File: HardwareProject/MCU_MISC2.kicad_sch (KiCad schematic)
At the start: 25 parts, among them J1 USB_B, J2 USB_C_Receptacle_USB2.0_16P, J3 Conn_02x16_Odd_Even, Q5 S8050, Q7 S8050, U5 TPD4E05U06DQA

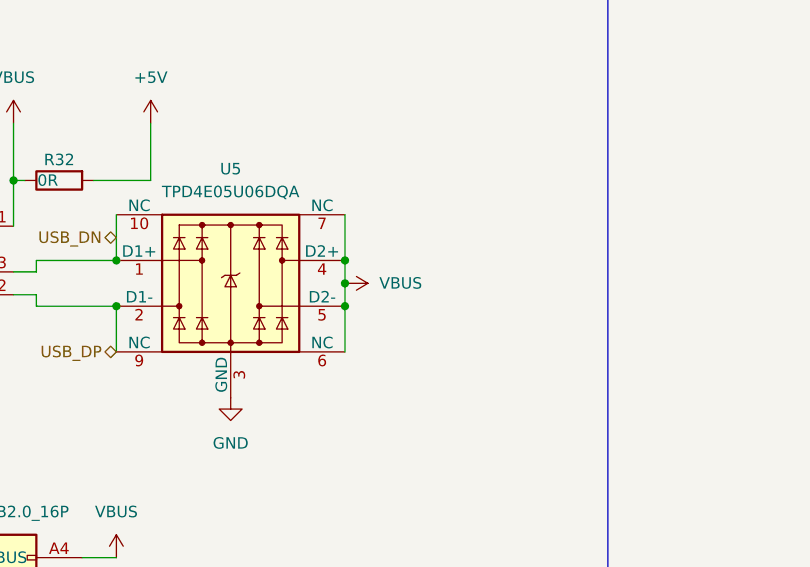
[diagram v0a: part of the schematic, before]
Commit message: 修改了UCC27211A封装，此芯片此前的封装均错误 修改了采样线布局，为SAR ADC加入前置RC
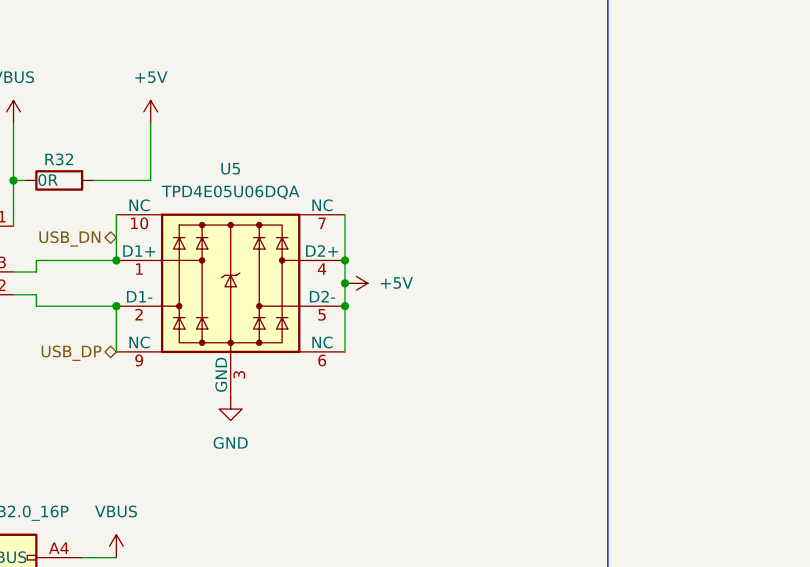
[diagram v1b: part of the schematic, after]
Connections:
- net +5V: now also U5.4 (D2+), U5.5 (D2-), U5.6 (NC), U5.7 (NC)
- net VBUS: no longer U5.4 (D2+), U5.5 (D2-), U5.6 (NC), U5.7 (NC)
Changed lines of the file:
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@@
 	)
 	(junction
+		(at 85.09 44.45)
+		(diameter 0)
+		(color 0 0 0 0)
+	)
+	(junction
 		(at 212.09 128.27)
 		(diameter 0)
@@
 	)
 	(junction
-		(at 85.09 44.45)
-		(diameter 0)
-		(color 0 0 0 0)
-	)
-	(junction
 		(at 201.93 41.91)
 		(diameter 0)
@@
 	(wire
 		(pts
+			(xy 85.09 44.45) (xy 85.09 46.99)
+		)
+		(stroke
+			(width 0)
+			(type default)
+		)
+	)
+	(wire
+		(pts
 			(xy 231.14 140.97) (xy 247.65 140.97)
 		)
@@
 	(wire
 		(pts
-			(xy 85.09 44.45) (xy 85.09 46.99)
+			(xy 85.09 41.91) (xy 85.09 44.45)
 		)
 		(stroke
@@
 	(wire
 		(pts
-			(xy 85.09 41.91) (xy 85.09 44.45)
-		)
-		(stroke
-			(width 0)
-			(type default)
-		)
-	)
-	(wire
-		(pts
 			(xy 50.8 157.48) (xy 50.8 151.13)
 		)
@@
 	)
 	(symbol
+		(lib_id "power:+5V")
+		(at 85.09 44.45 270)
+		(unit 1)
+		(exclude_from_sim no)
+		(in_bom yes)
+		(on_board yes)
+		(dnp no)
+		(fields_autoplaced yes)
+		(property "Reference" "#PWR075"
+			(at 81.28 44.45 0)
+			(effects
+				(font
+					(size 1.27 1.27)
+				)
+				(hide yes)
+			)
+		)
+		(property "Value" "+5V"
+			(at 88.9 44.4499 90)
+			(effects
+				(font
+					(size 1.27 1.27)
+				)
+				(justify left)
+			)
+		)
+		(property "Footprint" ""
+			(at 85.09 44.45 0)
+			(effects
+				(font
+					(size 1.27 1.27)
+				)
+				(hide yes)
+			)
+		)
+		(property "Datasheet" ""
+			(at 85.09 44.45 0)
+			(effects
+				(font
+					(size 1.27 1.27)
+				)
+				(hide yes)
+			)
+		)
+		(property "Description" ""
+			(at 85.09 44.45 0)
+			(effects
+				(font
+					(size 1.27 1.27)
+				)
+				(hide yes)
+			)
+		)
+		(pin "1"
+		)
+		(instances
+			(project "HPM6P41_BB"
+				(path "/714b8a30-f9a7-49d4-a000-bc20c4884c7a/8753c7ec-cb46-4092-8be3-4a324384953b"
+					(reference "#PWR075")
+					(unit 1)
+				)
+			)
+		)
+	)
+	(symbol
 		(lib_id "Device:R")
 		(at 46.99 157.48 90)
@@
 					(unit 1)
 				)
-			)
-		)
-	)
-	(symbol
-		(lib_id "power:VBUS")
-		(at 85.09 44.45 270)
-		(unit 1)
-		(exclude_from_sim no)
-		(in_bom yes)
-		(on_board yes)
-		(dnp no)
-		(fields_autoplaced yes)
-		(property "Reference" "#PWR075"
-			(at 81.28 44.45 0)
-			(effects
-				(font
-					(size 1.27 1.27)
-				)
-				(hide yes)
-			)
-		)
-		(property "Value" "VBUS"
-			(at 88.9 44.4499 90)
-			(effects
-				(font
-					(size 1.27 1.27)
-				)
-				(justify left)
-			)
-		)
-		(property "Footprint" ""
-			(at 85.09 44.45 0)
-			(effects
-				(font
-					(size 1.27 1.27)
-				)
-				(hide yes)
-			)
-		)
-		(property "Datasheet" ""
-			(at 85.09 44.45 0)
-			(effects
-				(font
-					(size 1.27 1.27)
-				)
-				(hide yes)
-			)
-		)
-		(property "Description" "Power symbol creates a global label with name \"VBUS\""
-			(at 85.09 44.45 0)
-			(effects
-				(font
-					(size 1.27 1.27)
-				)
-				(hide yes)
-			)
-		)
-		(pin "1"
-		)
-		(instances
-			(project "HPM6P41_BB"
-				(path "/714b8a30-f9a7-49d4-a000-bc20c4884c7a/8753c7ec-cb46-4092-8be3-4a324384953b"
-					(reference "#PWR075")
-					(unit 1)
-				)

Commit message: 外置核心电压SYR838以改善ADC噪声
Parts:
- R32, R70: value 0R -> 0Ω
- R72: value 100 -> 100Ω
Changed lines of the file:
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@@
 			)
 		)
-		(property "Value" "100"
+		(property "Value" "100Ω"
 			(at 57.15 151.13 90)
 			(effects
@@
 			)
 		)
-		(property "Value" "0R"
-			(at 43.18 135.89 90)
+		(property "Value" "0Ω"
+			(at 43.18 137.16 90)
 			(effects
 				(font
@@
 			)
 		)
-		(property "Value" "0R"
-			(at 52.07 33.02 90)
-			(effects
-				(font
+		(property "Value" "0Ω"
+			(at 53.34 33.02 90)
+			(effects
+				(font

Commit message: 换其他电感之前暂存一下
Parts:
- removed J1: USB_B, HPM6P41_BB:USB_B_OST_USB-B1HSxx_Horizontal, symbol Connector:USB_B
- removed J3: Conn_02x16_Odd_Even, Connector_PinHeader_2.54mm:PinHeader_2x16_P2.54mm_Vertical, symbol Connector_Generic:Conn_02x16_Odd_Even
- removed R32: 0Ω, Resistor_SMD:R_0805_2012Metric, symbol Device:R
- added C36, C39: 100nF, Capacitor_SMD:C_0603_1608Metric, symbol Device:C
- added C40, C41: 1uF,10V, Capacitor_SMD:C_0603_1608Metric, symbol Device:C
- added J1, J13, J14: 排针, Connector_PinHeader_2.54mm:PinHeader_1x02_P2.54mm_Vertical, symbol Connector:Conn_01x02_Pin
- added J4: Conn_ARM_JTAG_SWD_20, Connector_IDC:IDC-Header_2x10_P2.54mm_Vertical, symbol Connector:Conn_ARM_JTAG_SWD_20
- added U24: CA-IS3762HN, kicad_community_lib:CA-IS3762HN, symbol CA-IS3762HN:CA-IS3762HN
- added U26: XC6206PxxxMR, Package_TO_SOT_SMD:SOT-23-3, symbol Regulator_Linear:XC6206PxxxMR
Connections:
- net +3.3V: now also C39.2, U24.16 (VDDB)
- net +5V: now also J1.1 (Pin_1)
- net GND: now also C39.1, U24.9 (GNDB)
- net VBUS: now also J1.2 (Pin_2)
- new net 5V_SUPPLY: C40.1, J13.1 (Pin_1), J4.19 (DBGACK/NC), U26.3 (VI)
- new net CON_RX: J14.1 (Pin_1), U24.5 (VI4)
- new net CON_TCK: J4.9 (TCK/SWDCLK), U24.2 (VI1)
- new net CON_TDI: J4.5 (TDI), U24.4 (VI3)
- new net CON_TDO: J4.13 (TDO/SWO), U24.6 (VO5)
- new net CON_TMS: J4.7 (TMS/SWDIO), U24.3 (VI2)
- new net CON_TX: J14.2 (Pin_2), U24.7 (VO6)
- new net ISO_GND: C36.1, C40.2, C41.2, J13.2 (Pin_2), J4.10 (GND), J4.12 (GND), J4.14 (GND), J4.16 (GND), J4.18 (GND), J4.20 (GND), J4.4 (GND), J4.6 (GND), J4.8 (GND), U24.8 (GNDA), U26.1 (GND)
- new net ISO_RX: U24.12 (VO4)
- new net ISO_TX: U24.10 (VI6)
- new net TCK: U24.15 (VO1)
- new net TDI: U24.13 (VO3)
- new net TDO: U24.11 (VI5)
- new net TMS: U24.14 (VO2)
- new net VTREF: C36.2, C41.1, J4.1 (VTREF), U24.1 (VDDA), U26.2 (VO)
- no-connect marks 5 -> 10
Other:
- moved on the sheet: BZ1, C92, J2, Q7, R3, R30, R70, R71, R72, U5

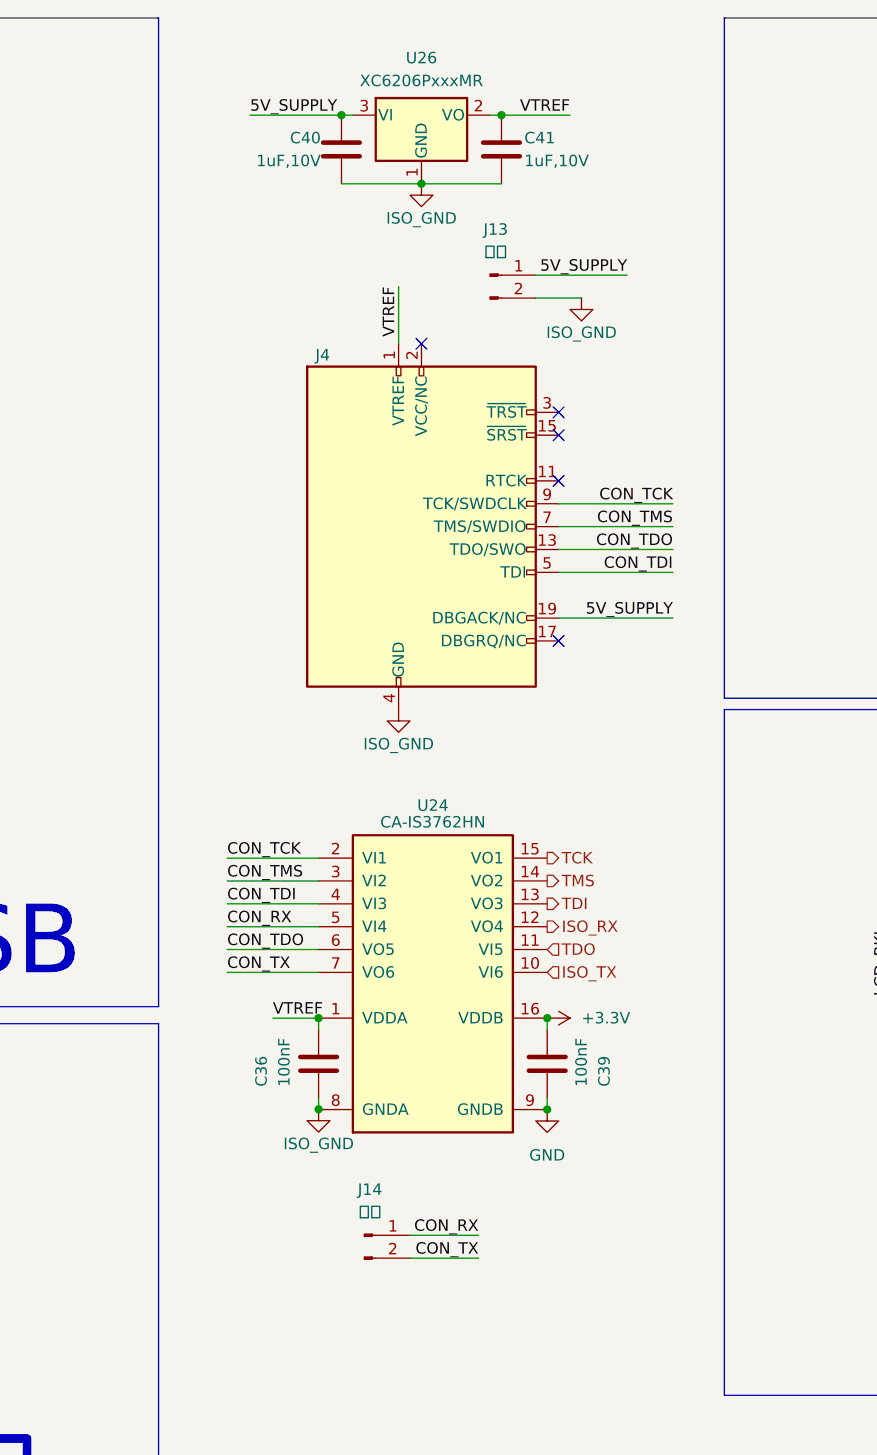
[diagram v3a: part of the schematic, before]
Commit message: 完成Rev4 电源 驱动 模拟 IO
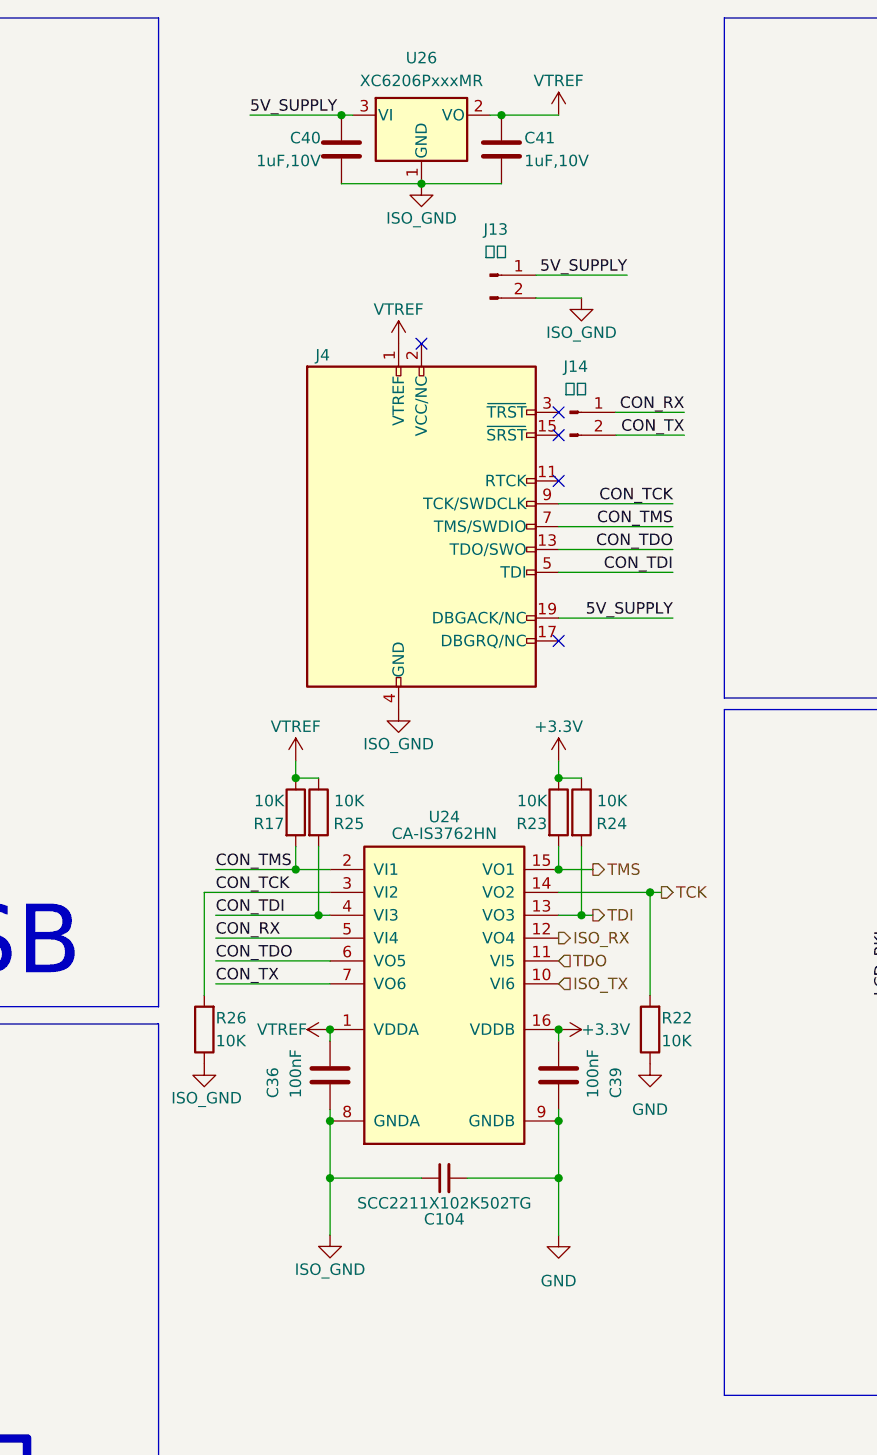
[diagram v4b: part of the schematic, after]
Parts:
- added C104: SCC2211X102K502TG, kicad_community_lib:SCC2211X102K502T, symbol SCC2211X102K502T:SCC2211X102K502T
- added R17, R22, R23, R24, R25, R26: 10K, Resistor_SMD:R_0603_1608Metric, symbol 02_HPM_Resistor:10K_0402
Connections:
- net +3.3V: now also R23.1, R24.1
- net CON_TCK: now also U24.3 (VI2), R26.2; no longer U24.2 (VI1)
- net CON_TDI: now also R25.2
- net CON_TMS: now also U24.2 (VI1), R17.2; no longer U24.3 (VI2)
- net GND: now also C104.2, R22.1
- net ISO_GND: now also C104.1, R26.1
- net TCK: now also U24.14 (VO2), R22.2; no longer U24.15 (VO1)
- net TDI: now also R24.2
- net TMS: now also U24.15 (VO1), R23.2; no longer U24.14 (VO2)
- net VTREF: now also R17.1, R25.1
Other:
- moved on the sheet: C36, C39, J14, U24

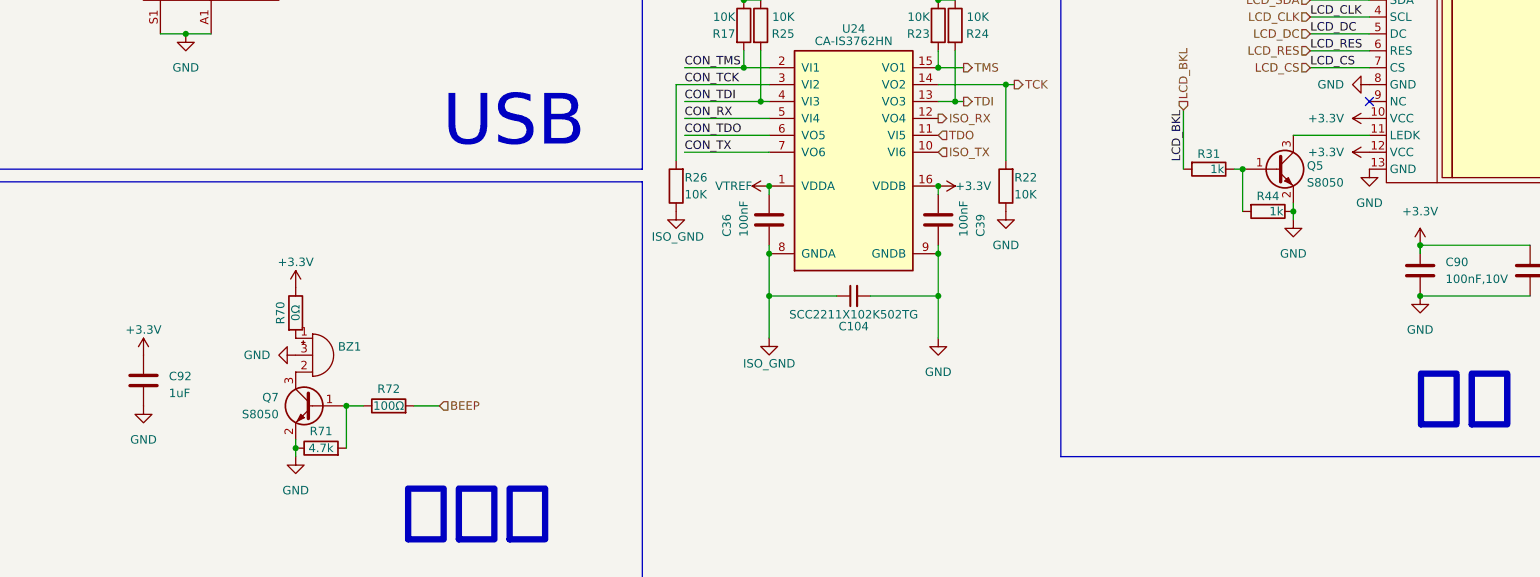
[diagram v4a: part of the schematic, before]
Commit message: 更新readme暂停通知，添加测试用例源代码
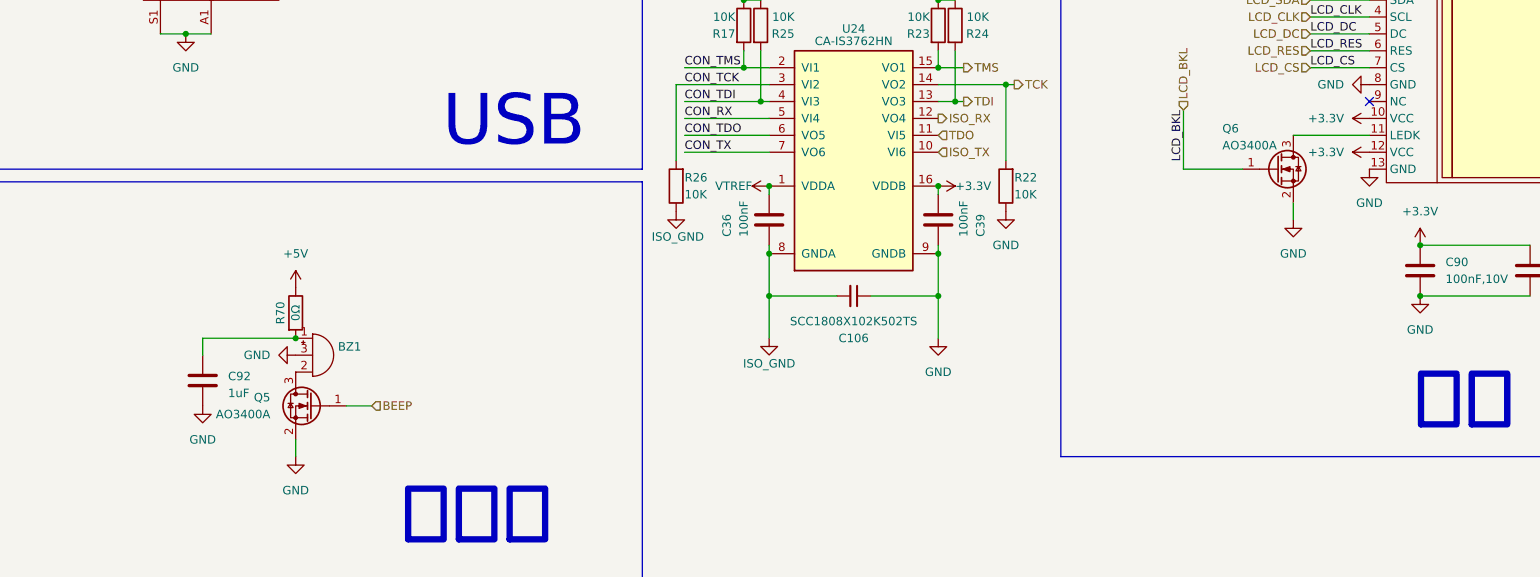
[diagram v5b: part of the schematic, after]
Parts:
- removed C104: SCC2211X102K502TG, kicad_community_lib:SCC2211X102K502T, symbol SCC2211X102K502T:SCC2211X102K502T
- removed Q5, Q7: S8050, Package_TO_SOT_SMD:SOT-23, symbol 1MyRandom:S8050
- removed R31, R44: 1k, Resistor_SMD:R_0603_1608Metric, symbol Device:R
- removed R71: 4.7k, Resistor_SMD:R_0603_1608Metric, symbol Device:R
- removed R72: 100Ω, Resistor_SMD:R_0603_1608Metric, symbol Device:R
- added C106: SCC1808X102K502TS, Capacitor_SMD:C_1808_4520Metric, symbol SCC1808X102K502TS:SCC1808X102K502TS
- added Q5, Q6: AO3400A, Package_TO_SOT_SMD:SOT-23, symbol Transistor_FET:AO3400A
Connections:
- net +3.3V: no longer C92.1, R70.1
- net +5V: now also R70.1
- net BEEP: now also Q5.1 (G)
- net GND: now also C106.1, Q5.2 (S), Q6.2 (S)
- net ISO_GND: now also C106.2
- net LCD_BKL: now also Q6.1 (G)
- net at S1.11 (LEDK): now also Q6.3 (D)
- net at BZ1.1 (+), R70.2: now also C92.1
- net at BZ1.2 (-): now also Q5.3 (D)
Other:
- moved on the sheet: C92

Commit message: rev4修改核心供电前保存（当前SYR838）
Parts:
- C76: renamed from C36; value 100nF -> 100nF,50V
- C80: renamed from C39; value 100nF -> 100nF,50V
- C81: renamed from C90; value 100nF,10V -> 100nF,50V
- C82: renamed from C91; value 100nF,10V -> 100nF,50V
- renumbered C92 to C75, C40 to C77, C106 to C78, C41 to C79, D11 to D18, D12 to D19, D15 to D20, J1 to J10, J4 to J11, J13 to J12, J14 to J13, J2 to J9, R70 to R66, R3 to R67, R30 to R68, R26 to R69, R17 to R70, R25 to R71, R23 to R72, R24 to R73, R22 to R74, R61 to R75, R62 to R76, R69 to R77, U5 to U23, U26 to U24, U24 to U25
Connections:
- net +5V: no longer U23.4 (D2+), U23.5 (D2-), U23.6 (NC), U23.7 (NC)
- net VBUS: now also U23.4 (D2+), U23.5 (D2-), U23.6 (NC), U23.7 (NC)

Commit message: Rev4保存
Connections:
- net VBUS: no longer U23.4 (D2+), U23.5 (D2-), U23.6 (NC), U23.7 (NC)
- new net: U23.4 (D2+), U23.5 (D2-), U23.6 (NC), U23.7 (NC)
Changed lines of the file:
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@@
 	)
 	(junction
-		(at 77.47 29.21)
-		(diameter 0)
-		(color 0 0 0 0)
-	)
-	(junction
 		(at 158.75 140.97)
 		(diameter 0)
@@
 	(wire
 		(pts
-			(xy 77.47 26.67) (xy 77.47 29.21)
+			(xy 77.47 26.67) (xy 77.47 31.75)
 		)
 		(stroke
@@
 	(wire
 		(pts
-			(xy 88.9 29.21) (xy 77.47 29.21)
-		)
-		(stroke
-			(width 0)
-			(type default)
-		)
-	)
-	(wire
-		(pts
 			(xy 143.51 30.48) (xy 152.4 30.48)
 		)
@@
 	(wire
 		(pts
-			(xy 77.47 29.21) (xy 77.47 31.75)
-		)
-		(stroke
-			(width 0)
-			(type default)
-		)
-	)
-	(wire
-		(pts
 			(xy 77.47 63.5) (xy 86.36 63.5)
 		)
@@
 					(unit 1)
 				)
-			)
-		)
-	)
-	(symbol
-		(lib_id "power:VBUS")
-		(at 88.9 29.21 0)
-		(unit 1)
-		(exclude_from_sim no)
-		(in_bom yes)
-		(on_board yes)
-		(dnp no)
-		(fields_autoplaced yes)
-		(property "Reference" "#PWR0155"
-			(at 88.9 33.02 0)
-			(effects
-				(font
-					(size 1.27 1.27)
-				)
-				(hide yes)
-			)
-		)
-		(property "Value" "VBUS"
-			(at 88.9 24.13 0)
-			(effects
-				(font
-					(size 1.27 1.27)
-				)
-			)
-		)
-		(property "Footprint" ""
-			(at 88.9 29.21 0)
-			(effects
-				(font
-					(size 1.27 1.27)
-				)
-				(hide yes)
-			)
-		)
-		(property "Datasheet" ""
-			(at 88.9 29.21 0)
-			(effects
-				(font
-					(size 1.27 1.27)
-				)
-				(hide yes)
-			)
-		)
-		(property "Description" "Power symbol creates a global label with name \"VBUS\""
-			(at 88.9 29.21 0)
-			(effects
-				(font
-					(size 1.27 1.27)
-				)
-				(hide yes)
-			)
-		)
-		(pin "1"
-		)
-		(instances
-			(project "HPM6P41_BB"
-				(path "/714b8a30-f9a7-49d4-a000-bc20c4884c7a/8753c7ec-cb46-4092-8be3-4a324384953b"
-					(reference "#PWR0155")
-					(unit 1)
-				)
